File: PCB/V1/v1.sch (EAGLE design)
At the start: 1 part

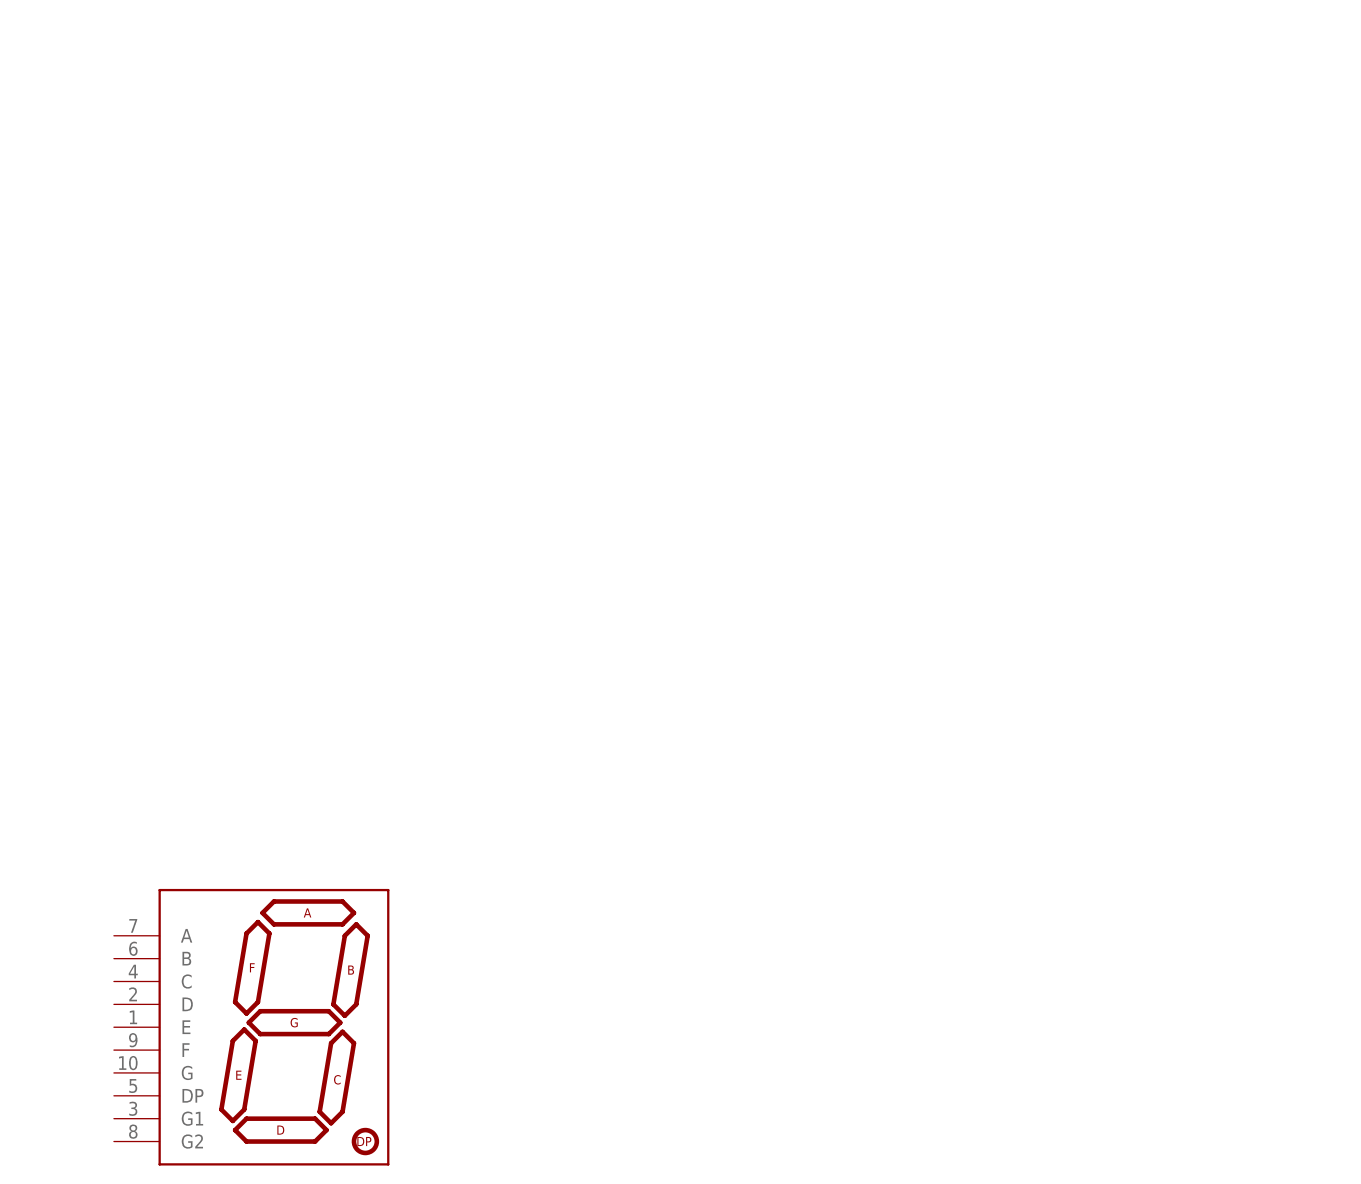
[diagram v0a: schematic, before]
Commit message: first pcb to test 7 segment, temperature sensor not added yet.
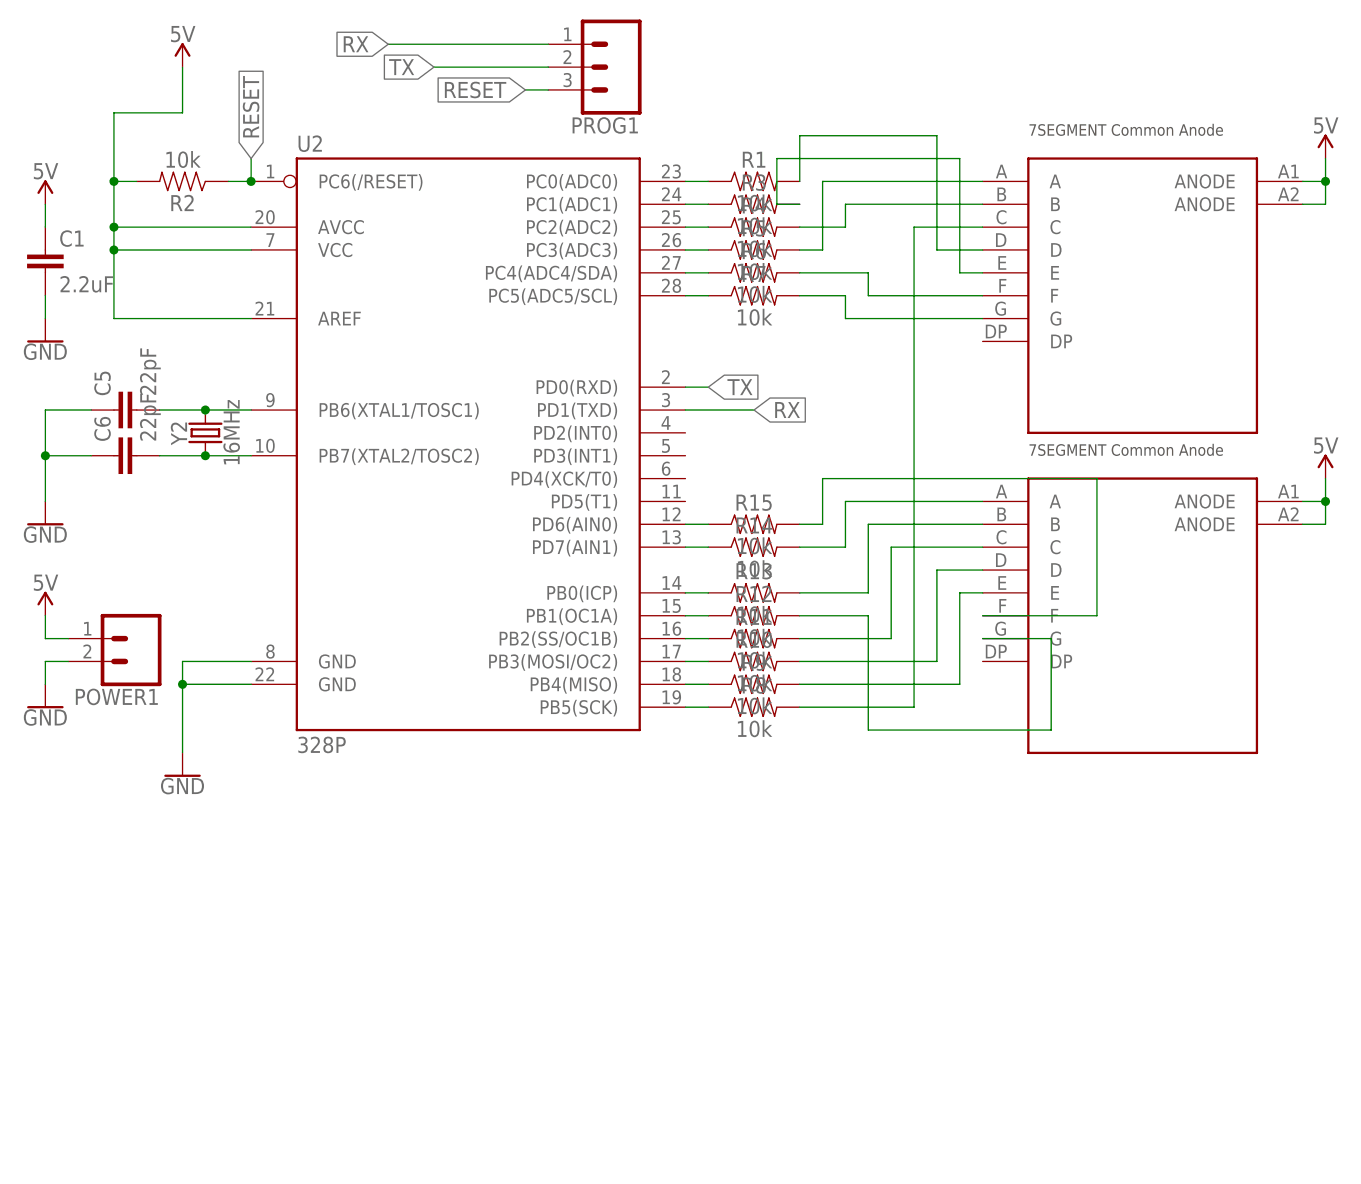
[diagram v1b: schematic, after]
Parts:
- added C1: 2.2uF, SparkFun-Capacitors:2.2UF-1206-50V-10%
- added C5, C6: 22pF, SparkFun-Capacitors:22PF-PTH-2.54MM-200V-5%
- added POWER1: (no value), SparkFun-Connectors:CONN_02
- added PROG1: (no value), SparkFun-Connectors:CONN_03
- added R1, R10, R11, R12, R13, R14, R15, R3, R4, R5, R6, R7, R8, R9: 10k, SparkFun-Resistors:0.22OHM-0805-1/4W-1%
- added R2: 10k, SparkFun-Resistors:1KOHM-HORIZ-1/4W-1%
- added U$2: 7SEGMENTCA, 7segmentca:7SEGMENTCA
- added U2: 328P, SparkFun-IC-Microcontroller:ATMEGA328P_PDIP
- added Y2: 16MHz, SparkFun-Clocks:CRYSTAL-16MHZPTH-HC49US
- U$1: value YSD-160AB3C-8 -> 7SEGMENTCA; device SparkFun-LED:7-SEGMENT-1DIGIT-1INCH-BLUE -> 7segmentca:7SEGMENTCA
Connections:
- new net 5V: C1.1, POWER1.1, R2.2, U$1.ANODE@3, U$1.ANODE@8, U$2.ANODE@3, U$2.ANODE@8, U2.AREF, U2.AVCC, U2.VCC
- new net GND: C1.2, C5.1, C6.1, POWER1.2, U2.GND@1, U2.GND@2
- new net N$1: C5.2, U2.PB6(XTAL1/TOSC1), Y2.2
- new net N$10: R6.2, U$1.F
- new net N$11: R5.2, U$1.A
- new net N$12: R4.2, U$1.B
- new net N$13: R3.2, U$1.E
- new net N$14: R1.2, U$1.D
- new net N$15: R8.1, U2.PB5(SCK)
- new net N$16: R8.2, U$1.C
- new net N$17: R12.1, U2.PB1(OC1A)
- new net N$18: R11.1, U2.PB2(SS/OC1B)
- new net N$19: R10.1, U2.PB3(MOSI/OC2)
- new net N$2: C6.2, U2.PB7(XTAL2/TOSC2), Y2.1
- new net N$20: R9.1, U2.PB4(MISO)
- new net N$21: R9.2, U$2.E
- new net N$22: R10.2, U$2.D
- new net N$23: R11.2, U$2.C
- new net N$24: R12.2, U$2.G
- new net N$25: R15.1, U2.PD6(AIN0)
- new net N$26: R14.1, U2.PD7(AIN1)
- new net N$27: R13.1, U2.PB0(ICP)
- new net N$28: R15.2, U$2.F
- new net N$29: R14.2, U$2.A
- new net N$3: R1.1, U2.PC0(ADC0)
- new net N$30: R13.2, U$2.B
- new net N$4: R3.1, U2.PC1(ADC1)
- new net N$5: R4.1, U2.PC2(ADC2)
- new net N$6: R5.1, U2.PC3(ADC3)
- new net N$7: R6.1, U2.PC4(ADC4/SDA)
- new net N$8: R7.1, U2.PC5(ADC5/SCL)
- new net N$9: R7.2, U$1.G
- new net RESET: PROG1.3, R2.1, U2.PC6(/RESET)
- new net RX: PROG1.1, U2.PD1(TXD)
- new net TX: PROG1.2, U2.PD0(RXD)
